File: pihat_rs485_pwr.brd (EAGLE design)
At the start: 49 x 42 mm, 39 parts, among them IC1 MAX481CSA, Q1 MOSFET-N2N7002, Q2 MOSFET-N2N7002, Q3 MOSFET-N2N7002

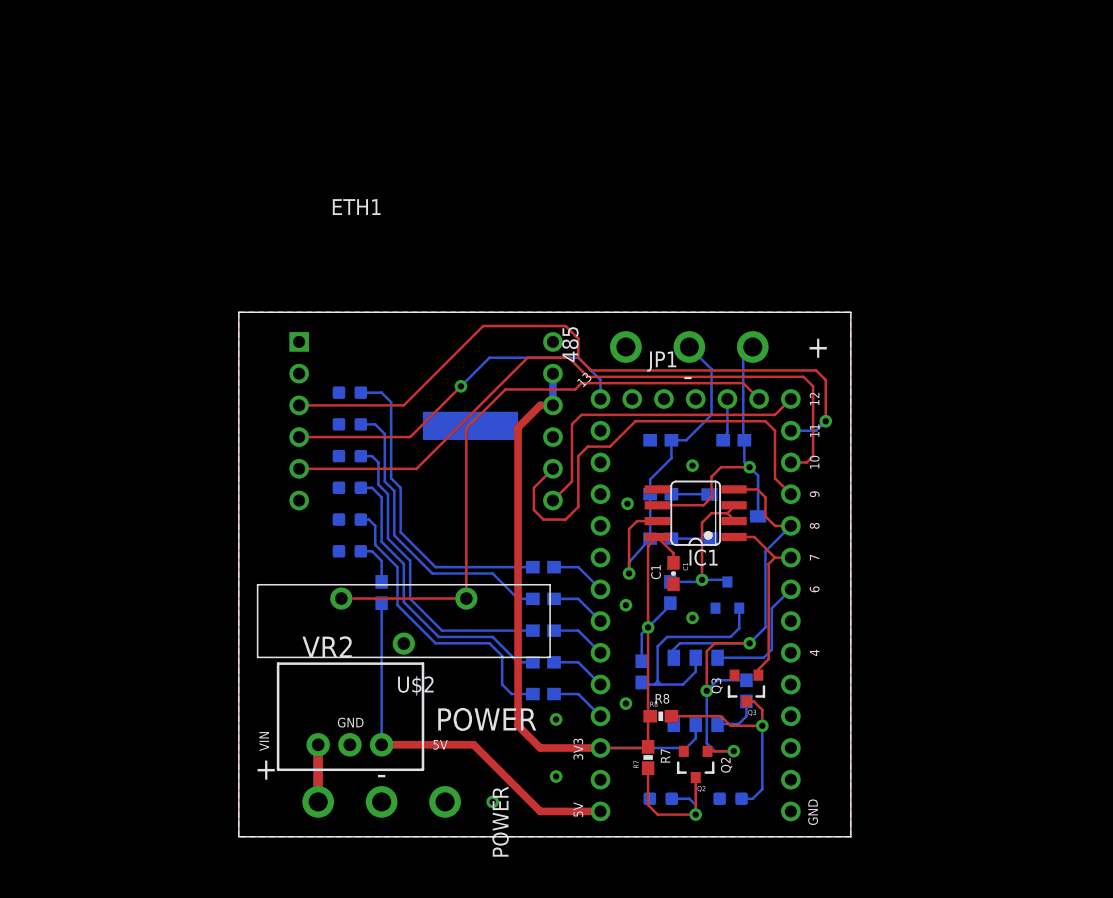
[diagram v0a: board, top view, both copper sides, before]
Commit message: 10/9/17, removed teensy, changed board dims
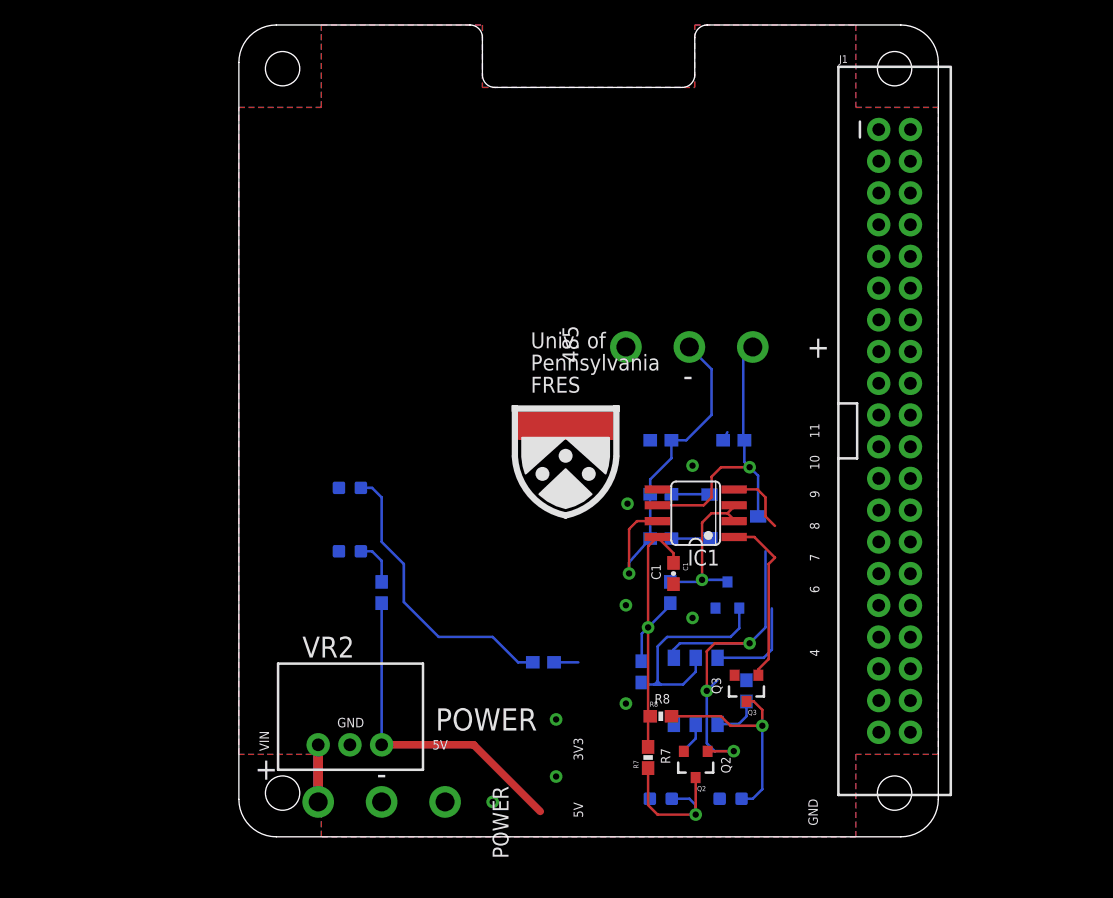
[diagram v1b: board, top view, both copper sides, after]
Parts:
- removed BATT, SDB: RED, SparkFun-LED:LED-0603
- removed EPW, SDW: YLW, SparkFun-LED:LED-0603
- removed ETH1: WIZ820IO_THIN, UPenn:WIZ820IO_THIN
- removed JP1: TEENSY_31_OUTER_THIN, UPenn:TEENSY-3.1_OUTER_THIN
- removed R1, R3, R4, R5: 680, SparkFun-Resistors:0603-RES
- removed U$1: WIZ820_SHLD_OVRLY, UPenn:WIZ820_SHLD_OVERLAY
- removed U$2: BATT_2POS_VERT, UPenn:BATTCONN_20MM_VERT
- added J1: RASPBERRYPI-40-PIN-GPIO_PTH, SparkFun-Connectors:2X20_SHROUDED
- RX, TX: value (none) -> YLW
- flipped U$4 to the top
- renumbered LED1 to TX, LED2 to RX
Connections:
- removed net N$10: ETH1.NRST, JP1.9
- removed net N$11: EPW.A, R5.2
- removed net N$18: BATT.A, R1.2
- removed net N$19: R3.2, SDB.A
- removed net N$21: R4.2, SDW.A
- removed net N$23: JP1.21, R3.1
- removed net N$24: JP1.20, R4.1
- removed net N$3: JP1.VBAT, U$2.POS@1, U$2.POS@2
- removed net N$4: JP1.19, R5.1
- removed net N$5: ETH1.NSS, JP1.10
- removed net N$6: ETH1.MOSI, JP1.11
- removed net N$7: ETH1.MISO, JP1.12
- removed net N$8: ETH1.SCLK, JP1.13
- removed net N$9: JP1.23, R1.1
- net 3.3V: now also J1.1, J1.17; no longer ETH1.3V3@7, ETH1.3V3@8, JP1.3.3V, JP1.3V
- net 5V: now also J1.2, J1.4; no longer JP1.VIN
- net GND: now also J1.14, J1.20, J1.25, J1.30, J1.34, J1.39, J1.6, J1.9; no longer BATT.C, EPW.C, ETH1.GND@0, ETH1.GND@1, ETH1.GND@6, ETH1.PWDN, JP1.AGND, JP1.GND, JP1.GND1, SDB.C, SDW.C, U$2.NEG
- net N$16: no longer JP1.7
- net N$17: no longer JP1.8
- net N$2: no longer JP1.6
- net N$22: no longer JP1.22
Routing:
- net N$6: track 53.9 -> 0.00 mm, vias 1 -> 0
- net N$5: track 53.4 -> 0.00 mm
- net 3.3V: track 79.1 -> 28.5 mm
- net N$3: track 49.1 -> 0.00 mm
- net N$10: track 35.1 -> 0.00 mm
- net N$8: track 29.0 -> 0.00 mm, vias 1 -> 0
- net N$11: track 25.2 -> 0.00 mm
- net N$7: track 25.1 -> 0.00 mm
- net N$19: track 24.5 -> 0.00 mm
- net N$21: track 23.9 -> 0.00 mm
- net N$18: track 23.6 -> 0.00 mm
- net N$17: track 43.6 -> 37.1 mm
- net 5V: track 31.1 -> 26.3 mm
- net N$24: track 4.46 -> 0.00 mm
- net N$23: track 4.46 -> 0.00 mm
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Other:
- board size 49 x 42 mm -> 56 x 65 mm
- board text removed: "12"
- board text removed: "13"

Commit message: 10/16/17, mostly set
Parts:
- removed VR2: R-78-E5.0, UPenn:R-78-EXX
- added C2: 1.0 uF, resistor:C0603
- added C3: 47 uF, resistor:C0603
- added R1: 10K, SparkFun-Resistors:0603
- added R3: 47K, SparkFun-Resistors:0603
- added U$1: MOSFET-P_SMD, UPenn:SOT23-3
- added U$2: FUSE, UPenn:1812_STD_BI
- added U$3: BIPOLAR_TRANS_ARRAY, UPenn:SOT363
- added U$5: DIODE_UNI, UPenn:DO-214AA_UNI
- added VR1: D24V22F5, UPenn:D24V22FX_FLAT
- C1: value 104 -> 0.1uF; device SparkFun-Capacitors:0603-CAP -> resistor:C0603
- J1: value RASPBERRYPI-40-PIN-GPIO_PTH -> RASPBERRYPI-40-PIN-GPIO_PTH_NO_SHROUND; device SparkFun-Connectors:2X20_SHROUDED -> UPenn:2X20
- R10, R11, R12, R13, R15, R2, R6, R7, R8, R9: device SparkFun-Resistors:0603-RES -> SparkFun-Resistors:0603
- R14: value 270 -> 180; device SparkFun-Resistors:0603-RES -> SparkFun-Resistors:0603
- moved RTCB 51.0 mm to (59.1, 36.9), flipped to the top
- moved R6 50.4 mm to (44.5, 57.7), flipped to the top
- moved PWR 48.0 mm to (41.1, 58.4), flipped to the top, turned to 180 degrees
- moved POWER 44.9 mm to (7.50, 47.6), turned to 90 degrees
- moved R2 44.8 mm to (61.4, 39.3), flipped to the top, turned to 180 degrees
- moved RX 35.6 mm to (22.9, 34.5), flipped to the top, turned to 0 degrees
- moved TX 32.0 mm to (27.9, 34.5), flipped to the top, turned to 0 degrees
- moved 485 30.7 mm to (7.50, 27.9), turned to 90 degrees
- moved R15 29.1 mm to (33.5, 39.9), flipped to the top, turned to 180 degrees
- moved U$4 27.5 mm to (10.2, 9.40)
- moved R11 27.0 mm to (12.7, 34.0), flipped to the top, turned to 270 degrees
- moved R7 25.6 mm to (27.9, 31.5), turned to 0 degrees
- moved R10 24.6 mm to (35.3, 37.6), flipped to the top, turned to 180 degrees
- moved R8 24.4 mm to (22.9, 31.5), turned to 180 degrees
- moved Q3 23.6 mm to (23.1, 27.7), turned to 90 degrees
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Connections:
- removed net N$17: IC1.4, Q2.1, R15.1, S1.6
- new net N$3: IC1.4, J1.8, Q2.1, R15.1, S1.6
- new net N$4: R1.2, U$3.2, U$3.5, U$3.6
- new net N$5: R3.2, U$1.1, U$3.3
- new net N$7: C2.1, U$1.3, U$2.2, U$3.1
- new net N$8: U$2.1, VR1.VOUT
- net 5V: now also C3.1, U$1.2, U$3.4, U$5.CA; no longer VR2.VOUT
- net GND: now also C2.2, C3.2, R1.1, R3.1, U$5.AN, VR1.GND; no longer VR2.GND
- net N$16: now also J1.10
- net N$2: now also J1.15
- net VIN: now also VR1.VIN; no longer VR2.VIN
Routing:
- net 3.3V: track 28.5 -> 86.1 mm, vias 1 -> 3
- net N$3: track 0.00 -> 51.2 mm
- net N$16: track 13.9 -> 56.4 mm
- net N$17: track 37.1 -> 0.00 mm, vias 3 -> 0
- net N$20: track 23.4 -> 0.00 mm
- net N$8: track 0.00 -> 19.1 mm
- net N$7: track 0.00 -> 11.5 mm
- net N$28: track 17.5 -> 6.87 mm, vias 1 -> 0
- net N$26: track 18.4 -> 8.88 mm
- net N$5: track 0.00 -> 8.03 mm
- net N$25: track 24.0 -> 31.6 mm, vias 1 -> 0
- net N$2: track 7.92 -> 15.0 mm
- net N$4: track 0.00 -> 6.38 mm
- net N$29: track 12.9 -> 6.87 mm, vias 1 -> 0
- net N$27: track 13.3 -> 18.4 mm, vias 1 -> 0
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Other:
- board text added: "BACnet-Modbus Gateway Rev 1.0"
- board text added: "Univ. of Pennsylvania FRES"
- board text removed: "10"
- board text removed: "11"
- board text removed: "4"
- board text removed: "6"
- board text removed: "7"
- board text removed: "8"
- board text removed: "9"
- board text removed: "BATT"
- board text removed: "EPW"
- board text removed: "FRES"
- board text removed: "Gateway"
- board text removed: "Modbus"
- board text removed: "Pennsylvania"
- board text removed: "R1"
- board text removed: "R3"
- board text removed: "R4"
- board text removed: "R5"
- board text removed: "Rev 2.1"
- board text removed: "SDB"
- board text removed: "SDW"
- board text removed: "Univ. of"

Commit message: 10/16/17, all silkscreens placed
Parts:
- removed U$1: MOSFET-P_SMD, UPenn:SOT23-3
- removed U$2: FUSE, UPenn:1812_STD_BI
- removed U$3: BIPOLAR_TRANS_ARRAY, UPenn:SOT363
- removed U$5: DIODE_UNI, UPenn:DO-214AA_UNI
- removed VR1: D24V22F5, UPenn:D24V22FX_FLAT
- added D1: DIODE_UNI, UPenn:DO-214AA_UNI
- added F1: FUSE, UPenn:1812_STD_BI
- added PS1: D24V22F5, UPenn:D24V22FX_FLAT
- added Q4: MOSFET-P_SMD, UPenn:SOT23-3
- added Q5: BIPOLAR_TRANS_ARRAY, UPenn:SOT363
- moved RTCB 49.7 mm to (13.5, 17.3), turned to 180 degrees
- moved R2 48.8 mm to (17.8, 17.3)
- moved PWR 19.0 mm to (35.1, 40.4)
- moved R6 17.8 mm to (40.1, 40.4), turned to 180 degrees
- moved U$4 4.79 mm to (7.62, 13.5)
- moved R1 4.19 mm to (43.7, 54.6), turned to 270 degrees
- moved R15 3.66 mm to (31.5, 36.8), turned to 270 degrees
- moved R3 3.05 mm to (43.7, 47.5)
- moved C2 2.90 mm to (36.1, 56.1), turned to 180 degrees
- moved S1 2.54 mm to (35.3, 30.5)
- moved Q1 2.54 mm to (41.7, 29.5)
- moved POWER 2.03 mm to (7.50, 49.6)
- moved C3 1.61 mm to (47.8, 59.2)
- moved R10 1.27 mm to (35.3, 36.3)
- moved C1 0.19 mm to (29.5, 17.3)
- renumbered IC1 to U1
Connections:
- net 5V: now also D1.CA, Q4.2, Q5.4; no longer U$1.2, U$3.4, U$5.CA
- net GND: now also D1.AN, PS1.GND; no longer U$5.AN, VR1.GND
- net N$22: now also J1.11
- net N$4: now also Q5.2, Q5.5, Q5.6; no longer U$3.2, U$3.5, U$3.6
- net N$5: now also Q4.1, Q5.3; no longer U$1.1, U$3.3
- net N$7: now also F1.2, Q4.3, Q5.1; no longer U$1.3, U$2.2, U$3.1
- net N$8: now also F1.1, PS1.VOUT; no longer U$2.1, VR1.VOUT
- net VIN: now also PS1.VIN; no longer VR1.VIN
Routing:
- net N$22: track 0.00 -> 56.9 mm, vias 0 -> 1
- net 5V: track 28.4 -> 42.9 mm
- net 3.3V: track 86.1 -> 89.7 mm
- net N$20: track 0.00 -> 2.59 mm
- net N$3: track 51.2 -> 53.4 mm
- net N$26: track 8.88 -> 10.1 mm
- net N$2: track 15.0 -> 16.0 mm
- net N$14: track 2.46 -> 3.35 mm
- net N$15: track 5.12 -> 4.25 mm
- net N$8: track 19.1 -> 20.0 mm
- net N$27: track 18.4 -> 19.1 mm
- net N$7: track 11.5 -> 12.1 mm
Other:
- board text added: "C"
- board text added: "C2"
- board text added: "C3"
- board text added: "D1"
- board text added: "EN"
- board text added: "F1"
- board text added: "G"
- board text added: "GPIO17"
- board text added: "GPIO22"
- board text added: "PG"
- board text added: "PIN_CTRL"
- board text added: "Q4"
- board text added: "Q5"
- board text added: "R1"
- board text added: "R3"
- board text added: "U1"
- board text added: "VOUT"
- board text removed: "D6_CTRL"
- board text removed: "RTCB"
